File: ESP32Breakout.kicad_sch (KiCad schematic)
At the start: 7 parts, among them J1 PIN6-9_Breakout, J2 PIN10-13_Breakout, U1 ESP32-S3

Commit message: Add indicator LEDs and digital +24VSafe detection line
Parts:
- added D8: LED-Y, LED_SMD:LED_0805_2012Metric, symbol Device:LED
- added R55: 1k, Resistor_SMD:R_0402_1005Metric, symbol Device:R_Small_US
- added R60: 270k, Resistor_SMD:R_0402_1005Metric, symbol Device:R_Small_US
- added R61: 33k, Resistor_SMD:R_0402_1005Metric, symbol Device:R_Small_US
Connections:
- net GND: now also D8.1 (K), R61.2
- net WIFI_INDICATOR: now reaches U1.21 (GPIO21)
- net WIFI_INDICATOR: now also R55.2
- net +24V_SAFE_DETECT: now reaches U1.38 (GPIO38)
- net +24V_SAFE_DETECT: now also R60.2, R61.1
- new net: D8.2 (A), R55.1
- new net +24V_SAFE: R60.1

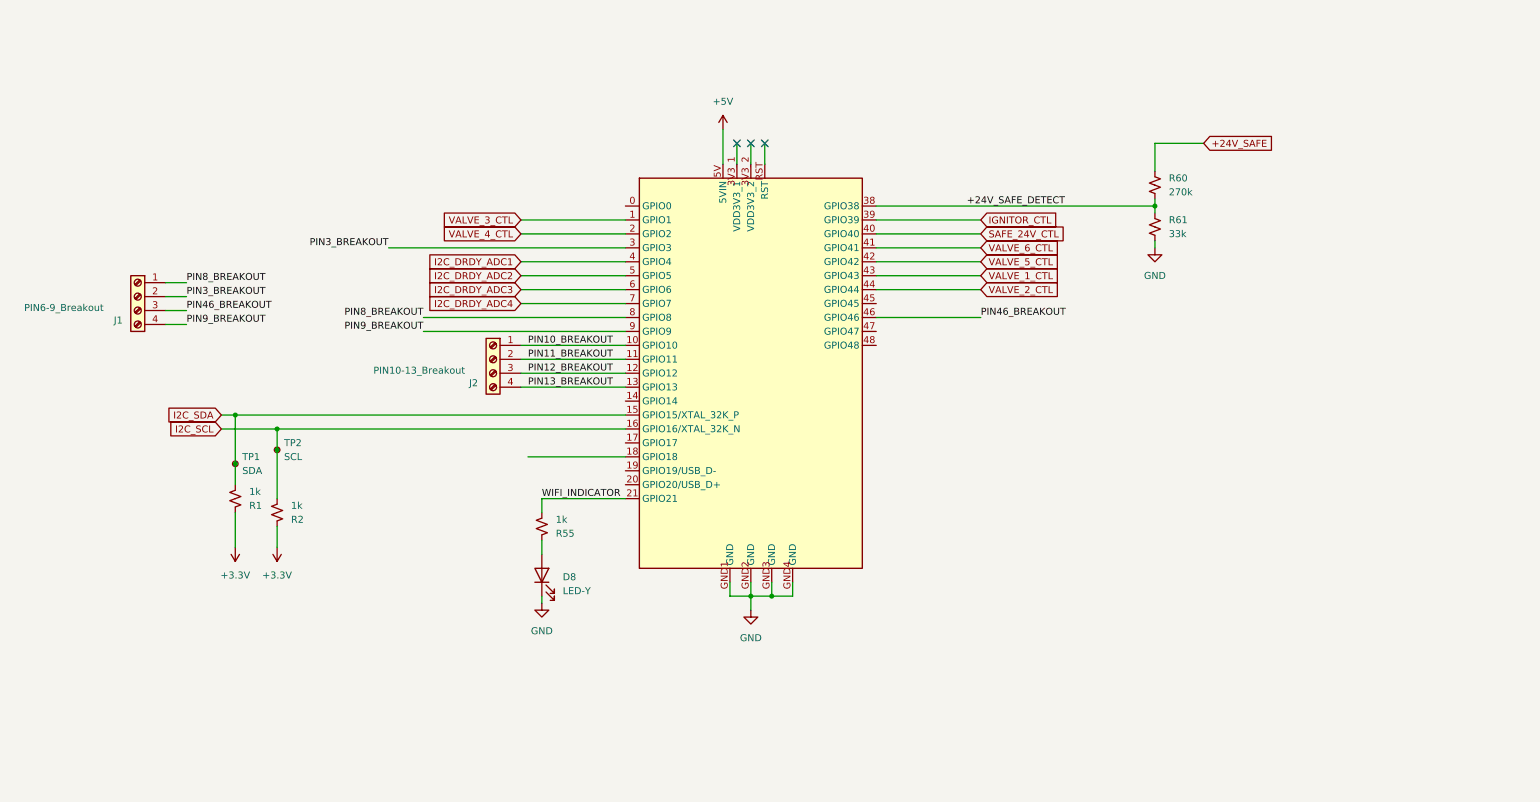
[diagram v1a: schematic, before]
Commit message: Completed necessary ESP32 wiring + new 3.3V LDO. GPIO pins not yet connected
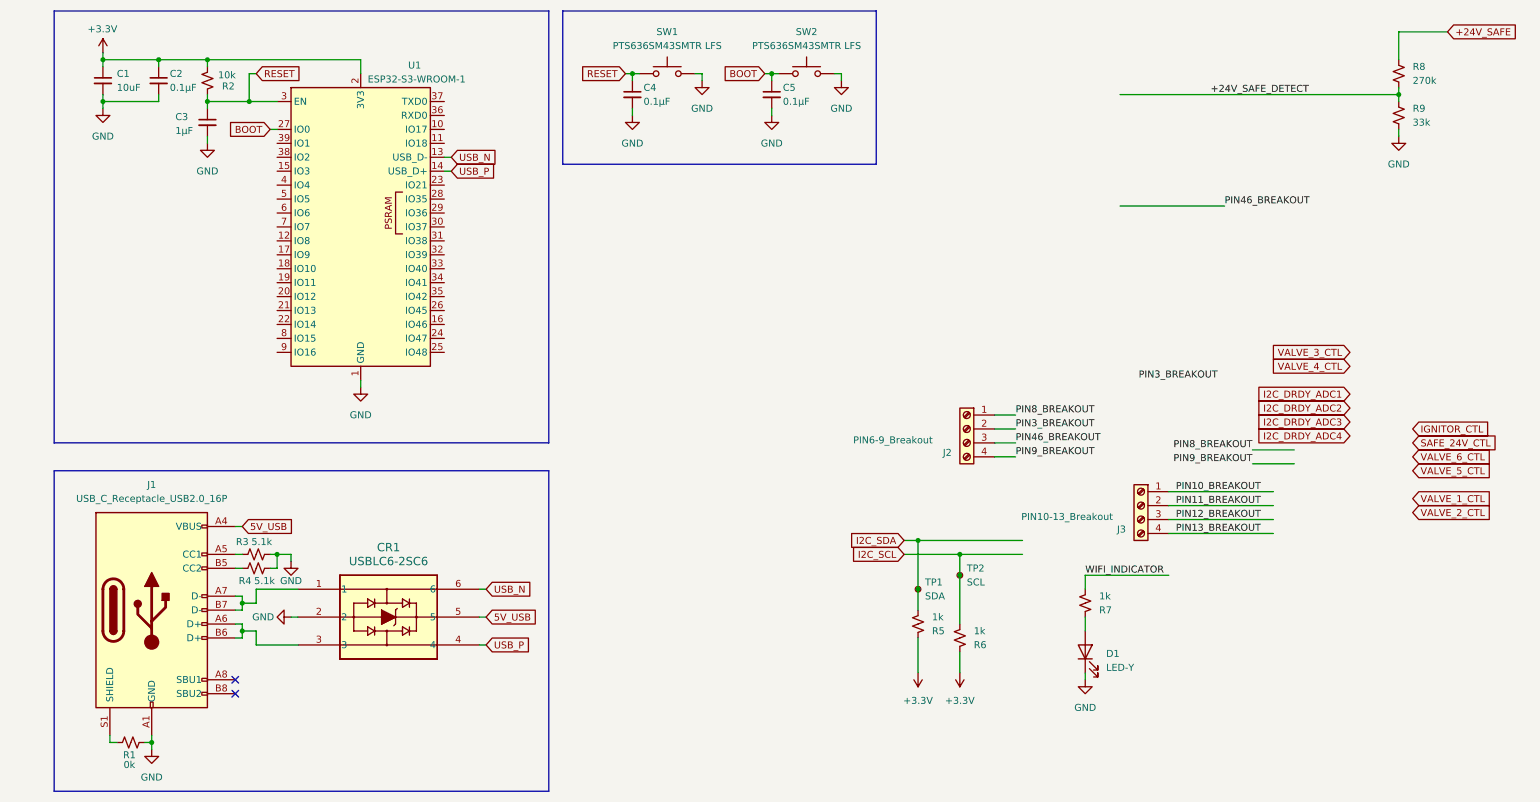
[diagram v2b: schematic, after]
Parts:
- removed U1: ESP32-S3, Library:ESP32_Devkit_C1_Noah, symbol ESP32_Devkit_C1_Noah:ESP32-S3
- added C1: 10uF, Capacitor_SMD:C_1206_3216Metric, symbol Device:C_Small
- added C2, C4, C5: 0.1μF, Capacitor_SMD:C_0402_1005Metric, symbol Device:C_Small
- added C3: 1μF, Capacitor_SMD:C_0402_1005Metric, symbol Device:C_Small
- added CR1: USBLC6-2SC6, Package_TO_SOT_SMD:SOT-23-6, symbol USBLC6-2SC6:USBLC6-2SC6
- added J1: USB_C_Receptacle_USB2.0_16P, symbol Connector:USB_C_Receptacle_USB2.0_16P
- added R1: 0k, Resistor_SMD:R_0402_1005Metric, symbol Device:R_Small_US
- added R2: 10k, Resistor_SMD:R_0402_1005Metric, symbol Device:R_Small_US
- added R3, R4: 5.1k, Resistor_SMD:R_0402_1005Metric, symbol Device:R_Small_US
- added SW1, SW2: PTS636SM43SMTR LFS, Button_Switch_SMD:SW_Tactile_SPST_NO_Straight_CK_PTS636Sx25SMTRLFS, symbol Switch:SW_Push
- added U1: ESP32-S3-WROOM-1, RF_Module:ESP32-S3-WROOM-1, symbol RF_Module:ESP32-S3-WROOM-1
- renumbered D8 to D1, J1 to J2, J2 to J3, R1 to R5, R2 to R6, R55 to R7, R60 to R8, R61 to R9
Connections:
- net +3.3V: now also C1.1, C2.1, R2.2, U1.2 (3V3)
- net GND: now also C1.2, C2.2, C3.2, C4.2, C5.2, CR1.2, J1.A1 (GND), J1.A12 (GND), J1.B1 (GND), J1.B12 (GND), R1.2, R3.2, R4.2, SW1.2, SW2.2, U1.1 (GND), U1.40 (GND), U1.41 (GND)
- new net: J1.A5 (CC1), R3.1
- new net: J1.B5 (CC2), R4.1
- new net: J1.S1 (SHIELD), R1.1
- new net: CR1.3, J1.A6 (D+), J1.B6 (D+)
- new net: CR1.1, J1.A7 (D-), J1.B7 (D-)
- new net 5V_USB: CR1.5, J1.A4 (VBUS), J1.A9 (VBUS), J1.B4 (VBUS), J1.B9 (VBUS)
- new net BOOT: C5.1, SW2.1, U1.27 (IO0)
- new net RESET: C3.1, C4.1, R2.1, SW1.1, U1.3 (EN)
- new net USB_N: CR1.6, U1.13 (USB_D-)
- new net USB_P: CR1.4, U1.14 (USB_D+)
- no-connect marks 3 -> 2
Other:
- moved on the sheet: D1, J2, J3, R5, R6, R7, R8, R9, TP1, TP2

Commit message: connected to GPIO pins
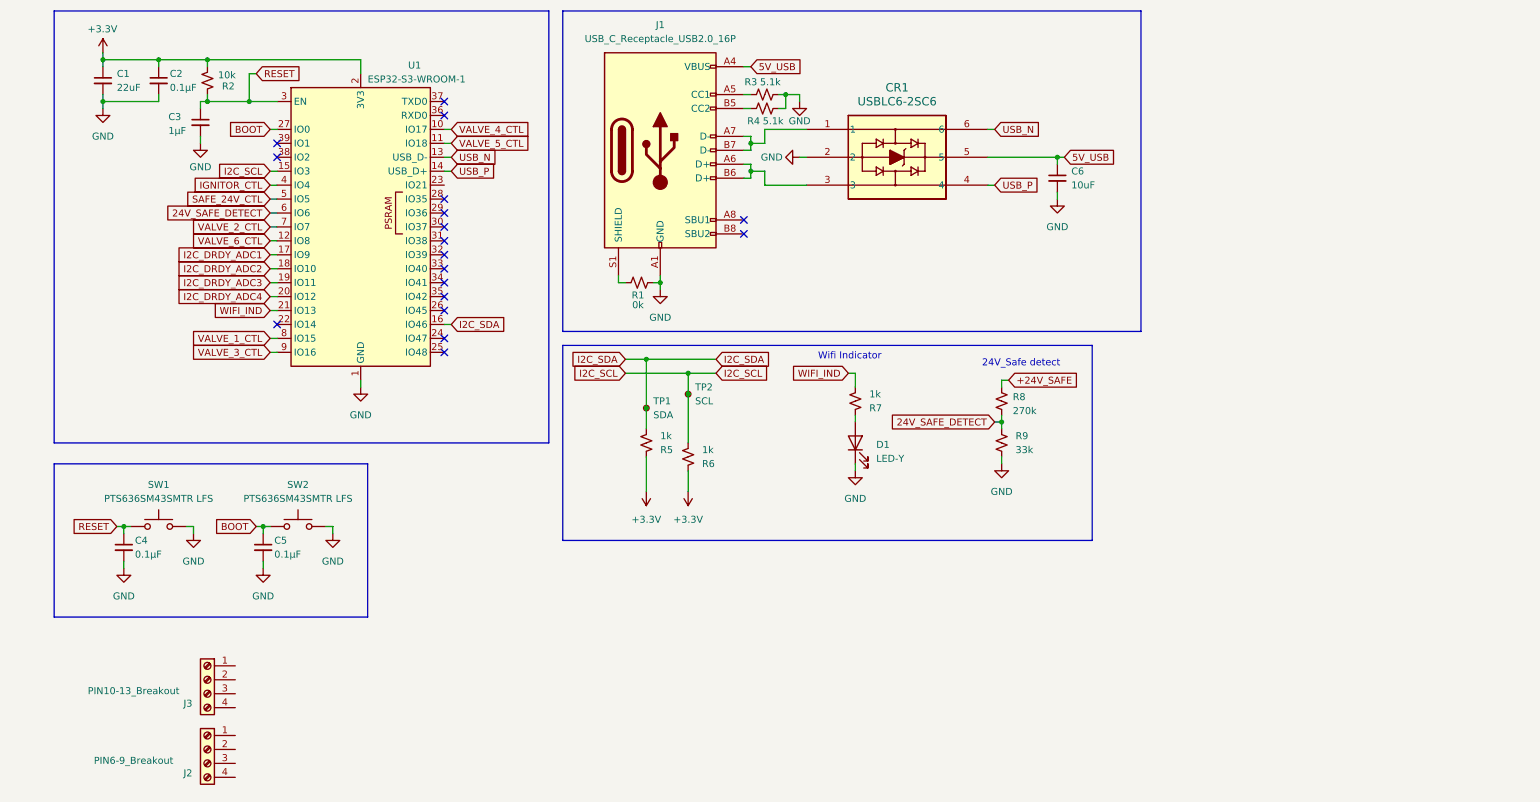
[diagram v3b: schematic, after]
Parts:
- added C6: 10uF, Capacitor_SMD:C_1206_3216Metric, symbol Device:C_Small
- C1: value 10uF -> 22uF
- J1: footprint (none) -> Connector_USB:USB_C_Receptacle_HCTL_HC-TYPE-C-16P-01A
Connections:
- net +24V_SAFE_DETECT is gone; now on net 24V_SAFE_DETECT: R8.2, R9.1
- net WIFI_INDICATOR is gone; now on net WIFI_IND: R7.2
- net 5V_USB: now also C6.1
- net GND: now also C6.2
- net I2C_DRDY_ADC1: now also U1.17 (IO9)
- net I2C_DRDY_ADC2: now also U1.18 (IO10)
- net I2C_DRDY_ADC3: now also U1.19 (IO11)
- net I2C_DRDY_ADC4: now also U1.20 (IO12)
- net I2C_SCL: now also U1.15 (IO3)
- net I2C_SDA: now also U1.16 (IO46)
- net IGNITOR_CTL: now also U1.4 (IO4)
- net SAFE_24V_CTL: now also U1.5 (IO5)
- net VALVE_1_CTL: now also U1.8 (IO15)
- net VALVE_2_CTL: now also U1.7 (IO7)
- net VALVE_3_CTL: now also U1.9 (IO16)
- net VALVE_4_CTL: now also U1.10 (IO17)
- net VALVE_5_CTL: now also U1.11 (IO18)
- net VALVE_6_CTL: now also U1.12 (IO8)
- net WIFI_IND: now reaches U1.21 (IO13)
- net 24V_SAFE_DETECT: now reaches U1.6 (IO6)
- net PIN10_BREAKOUT: no longer names the net of J3.1 (Pin_1)
- net PIN11_BREAKOUT: no longer names the net of J3.2 (Pin_2)
- net PIN12_BREAKOUT: no longer names the net of J3.3 (Pin_3)
- net PIN13_BREAKOUT: no longer names the net of J3.4 (Pin_4)
- net PIN3_BREAKOUT: no longer names the net of J2.2 (Pin_2)
- net PIN46_BREAKOUT: no longer names the net of J2.3 (Pin_3)
- net PIN8_BREAKOUT: no longer names the net of J2.1 (Pin_1)
- net PIN9_BREAKOUT: no longer names the net of J2.4 (Pin_4)
- no-connect marks 2 -> 18
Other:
- note added: "24V_Safe detect"
- note added: "Wifi Indicator"
- moved on the sheet: C3, C4, C5, CR1, D1, J1, J2, J3, R1, R3, R4, R5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

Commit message: added 24V lockout key LED indicator
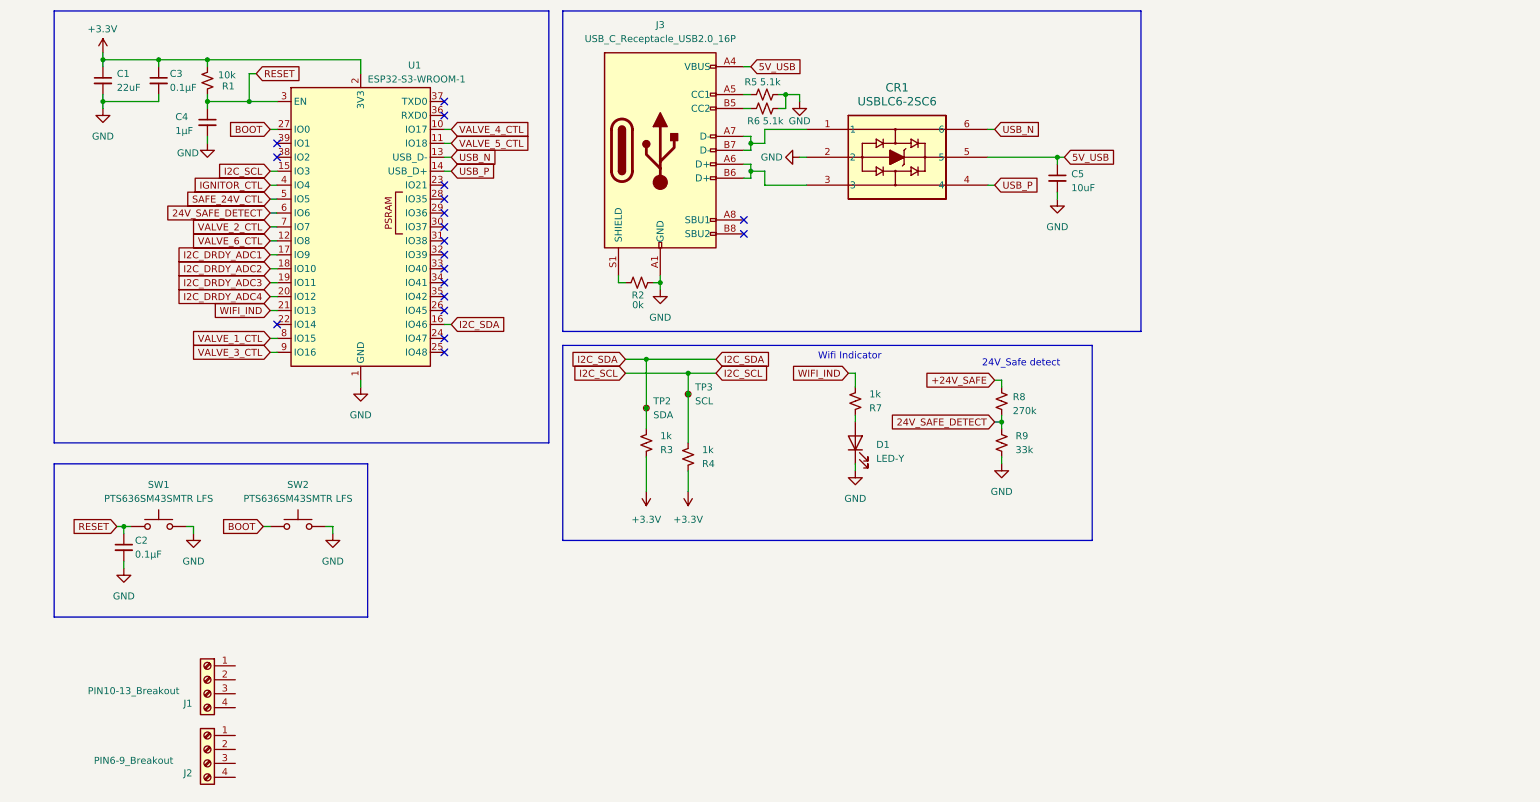
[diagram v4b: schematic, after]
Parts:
- removed C5: 0.1μF, Capacitor_SMD:C_0402_1005Metric, symbol Device:C_Small
- renumbered C4 to C2, C2 to C3, C3 to C4, C6 to C5, J3 to J1, J1 to J3, R2 to R1, R1 to R2, R5 to R3, R6 to R4, R3 to R5, R4 to R6, TP1 to TP2, TP2 to TP3
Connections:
- no-connect marks 18 -> 19
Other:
- moved on the sheet: C4

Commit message: pcb first draft, changed esp32 pin connections
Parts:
- removed J2: PIN6-9_Breakout, TerminalBlock:TerminalBlock_Xinya_XY308-2.54-4P_1x04_P2.54mm_Horizontal, symbol Connector:Screw_Terminal_01x04
- removed R2: 0k, Resistor_SMD:R_0402_1005Metric, symbol Device:R_Small_US
- C5: value 10uF -> 0.1uF; footprint Capacitor_SMD:C_1206_3216Metric -> Capacitor_SMD:C_0402_1005Metric
- renumbered R3 to R2, R4 to R3, R5 to R4, R6 to R5, R7 to R6, R8 to R7, R9 to R8
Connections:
- net I2C_SCL: now also U1.16 (IO46); no longer U1.15 (IO3)
- net I2C_SDA: now also U1.15 (IO3); no longer U1.16 (IO46)
- net IGNITOR_CTL: now also U1.5 (IO5); no longer U1.4 (IO4)
- net SAFE_24V_CTL: now also U1.4 (IO4); no longer U1.5 (IO5)
- net VALVE_1_CTL: now also U1.7 (IO7); no longer U1.8 (IO15)
- net VALVE_2_CTL: now also U1.8 (IO15); no longer U1.7 (IO7)
- net VALVE_3_CTL: now also U1.12 (IO8); no longer U1.9 (IO16)
- net VALVE_4_CTL: now also U1.11 (IO18); no longer U1.10 (IO17)
- net VALVE_5_CTL: now also U1.10 (IO17); no longer U1.11 (IO18)
- net VALVE_6_CTL: now also U1.9 (IO16); no longer U1.12 (IO8)
- net MTMS: now reaches J1.1 (Pin_1)
- net MTMS: now also U1.35 (IO42)
- net MTDI: now reaches J1.2 (Pin_2)
- net MTDI: now also U1.34 (IO41)
- net MTDO: now reaches J1.3 (Pin_3)
- net MTDO: now also U1.33 (IO40)
- net MTCK: now reaches J1.4 (Pin_4)
- net MTCK: now also U1.32 (IO39)
- no-connect marks 19 -> 16
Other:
- moved on the sheet: J1
